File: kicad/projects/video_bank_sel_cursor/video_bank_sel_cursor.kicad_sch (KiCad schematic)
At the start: 44 parts, among them J1 peripheral_addr_bus_connector, J2 peripheral_aux_connector, J3 peripheral_membank_connector, J4 Conn_01x16_Socket, J5 Conn_01x16_Socket, J6 video_aux, J7 Conn_01x16_Socket, J8 Conn_01x06_Socket, U1 74HC245, U10 74HC10, U11 74HC377, U12 74HC377, U14 74HC245, U15 74HC245, U2 74HC245, U3 74HC245, U4 74HC245, U5 74HC245, U6 74HC245, U7 74HC245, U8 74HC245, U9 74HC10

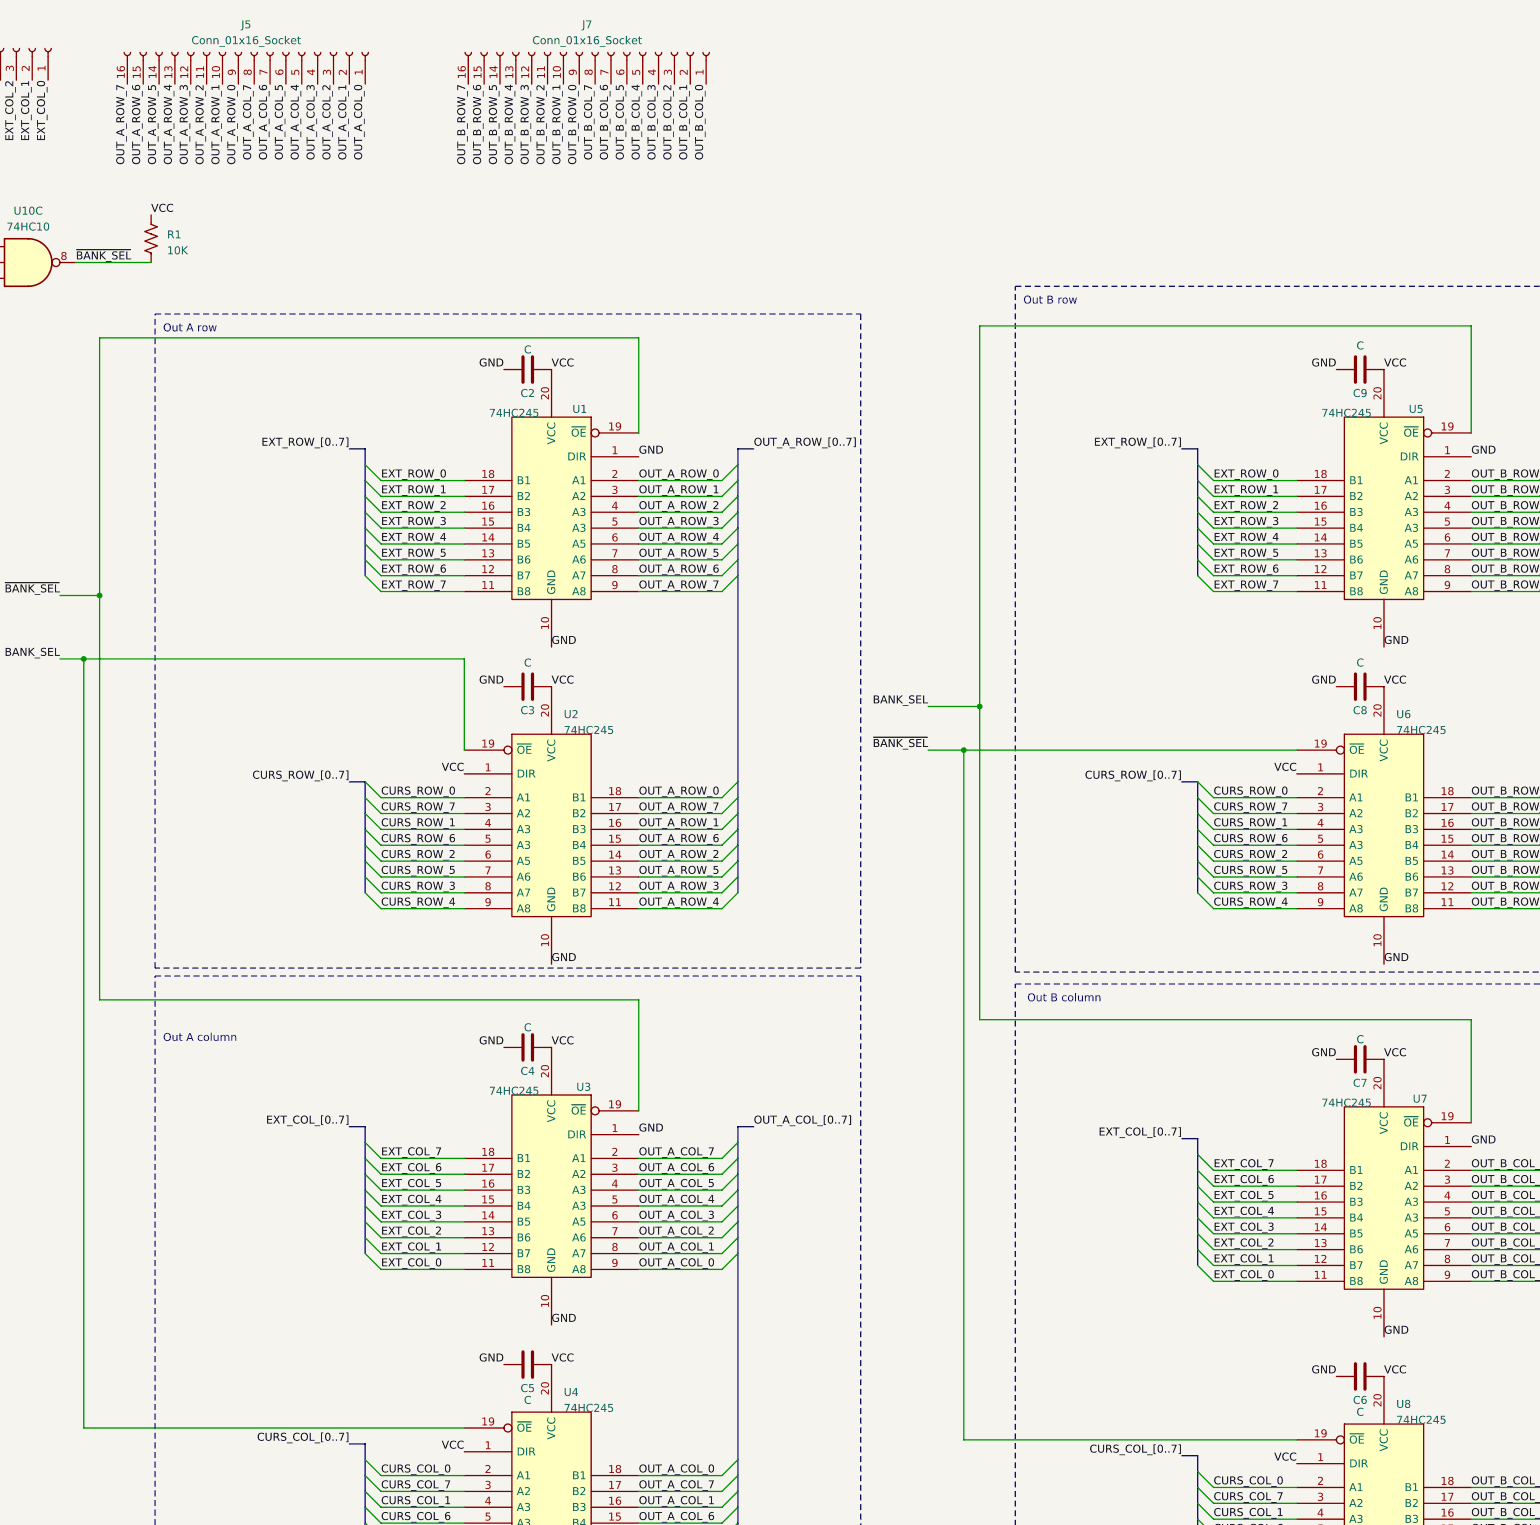
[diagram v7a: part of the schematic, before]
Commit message: Switched A and B outputs on bank sel. Bit of work on logic and PCB for output. Clarified bank sel 0 and 1 and banks A and B in docs.
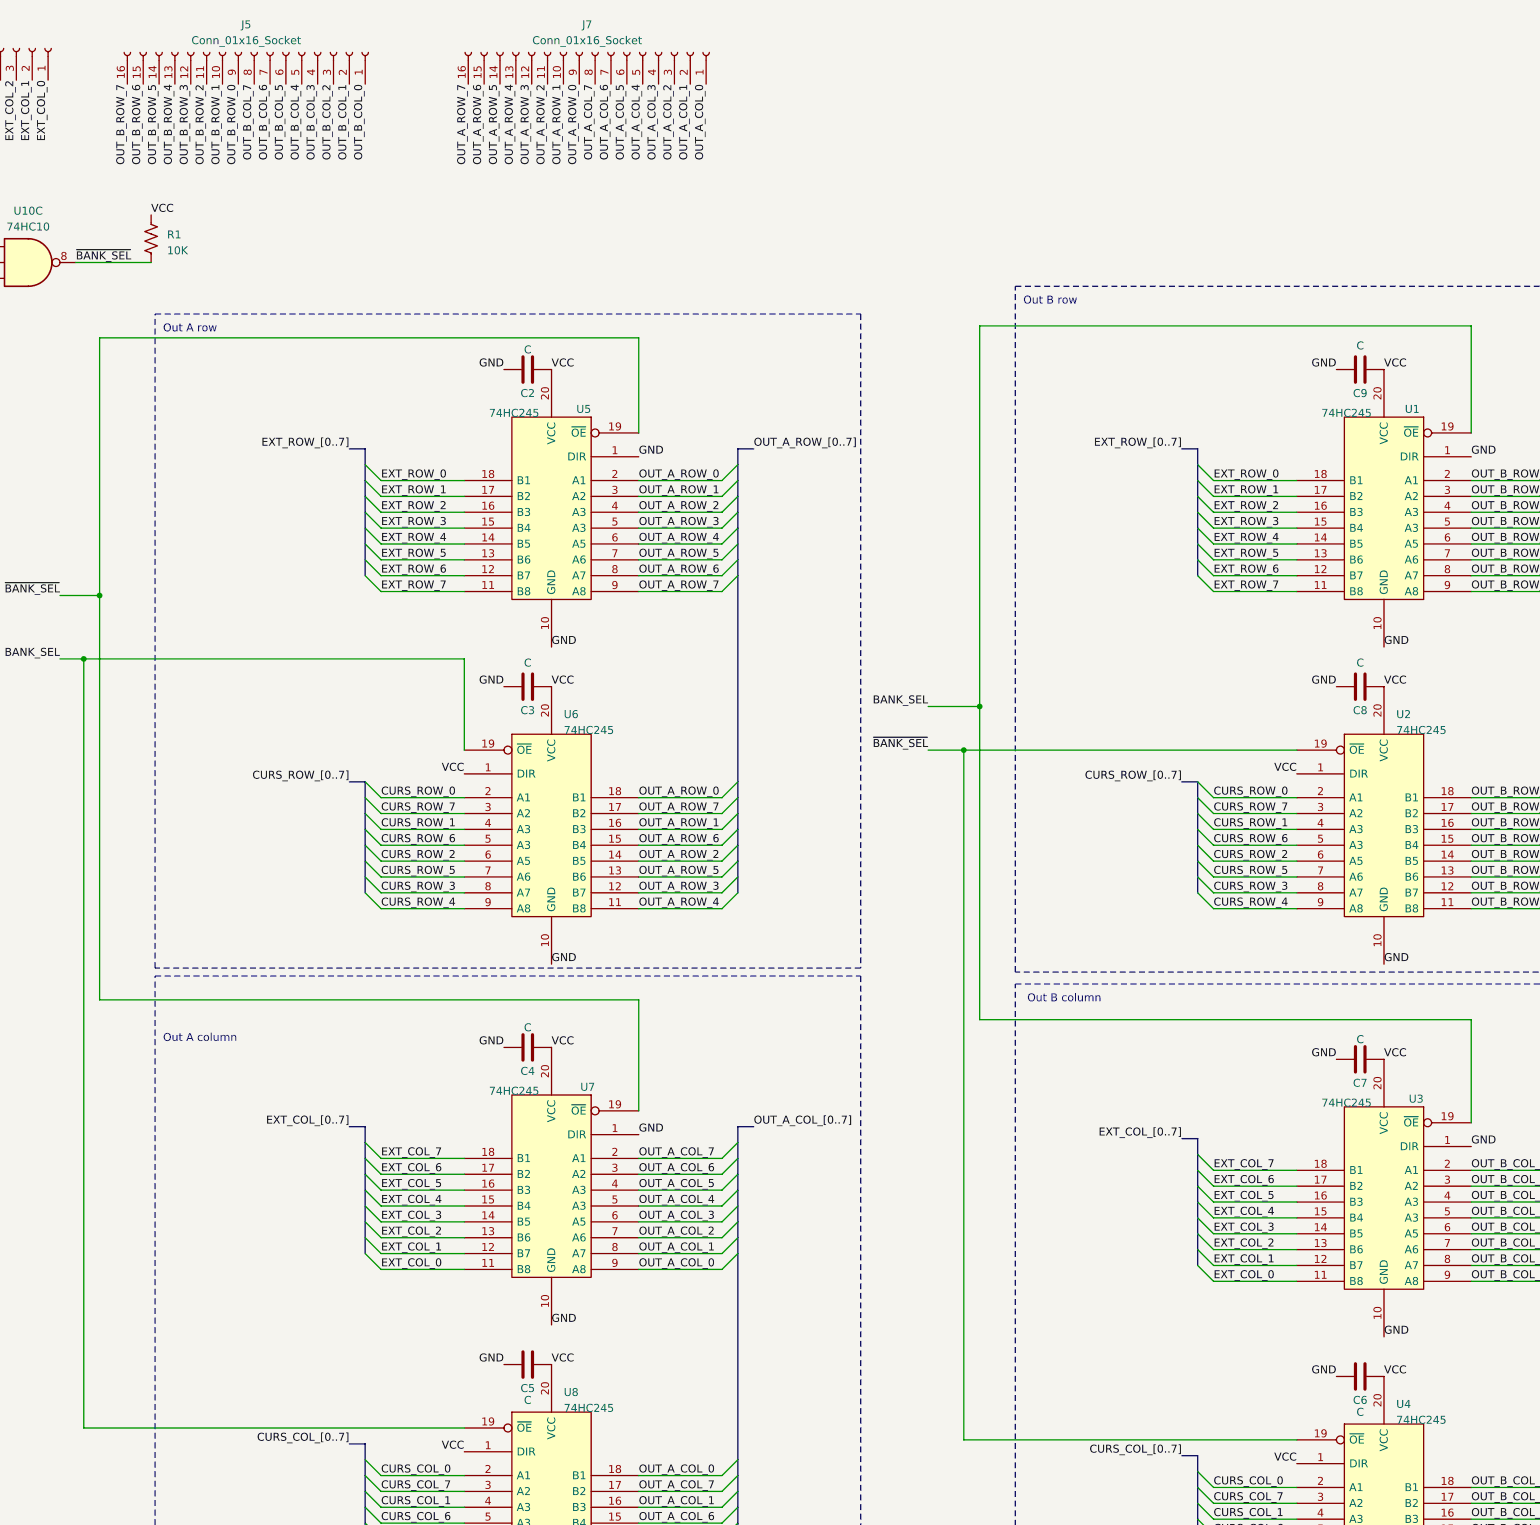
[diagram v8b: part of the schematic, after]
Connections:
- net BANK_SEL: now also U1.19 (~{OE}), U3.19 (~{OE}), U6.19 (~{OE}), U8.19 (~{OE}); no longer U2.19 (~{OE}), U4.19 (~{OE}), U5.19 (~{OE}), U7.19 (~{OE})
- net OUT_A_COL_0: now also J7.1 (Pin_1), U7.9 (A8), U8.18 (B1); no longer J5.1 (Pin_1), U3.9 (A8), U4.18 (B1)
- net OUT_A_COL_1: now also J7.2 (Pin_2), U7.8 (A7), U8.16 (B3); no longer J5.2 (Pin_2), U3.8 (A7), U4.16 (B3)
- net OUT_A_COL_2: now also J7.3 (Pin_3), U7.7 (A6), U8.14 (B5); no longer J5.3 (Pin_3), U3.7 (A6), U4.14 (B5)
- net OUT_A_COL_3: now also J7.4 (Pin_4), U7.6 (A5), U8.12 (B7); no longer J5.4 (Pin_4), U3.6 (A5), U4.12 (B7)
- net OUT_A_COL_4: now also J7.5 (Pin_5), U7.5 (A3), U8.11 (B8); no longer J5.5 (Pin_5), U3.5 (A3), U4.11 (B8)
- net OUT_A_COL_5: now also J7.6 (Pin_6), U7.4 (A3), U8.13 (B6); no longer J5.6 (Pin_6), U3.4 (A3), U4.13 (B6)
- net OUT_A_COL_6: now also J7.7 (Pin_7), U7.3 (A2), U8.15 (B4); no longer J5.7 (Pin_7), U3.3 (A2), U4.15 (B4)
- net OUT_A_COL_7: now also J7.8 (Pin_8), U7.2 (A1), U8.17 (B2); no longer J5.8 (Pin_8), U3.2 (A1), U4.17 (B2)
- net OUT_A_ROW_0: now also J7.9 (Pin_9), U5.2 (A1), U6.18 (B1); no longer J5.9 (Pin_9), U1.2 (A1), U2.18 (B1)
- net OUT_A_ROW_1: now also J7.10 (Pin_10), U5.3 (A2), U6.16 (B3); no longer J5.10 (Pin_10), U1.3 (A2), U2.16 (B3)
- net OUT_A_ROW_2: now also J7.11 (Pin_11), U5.4 (A3), U6.14 (B5); no longer J5.11 (Pin_11), U1.4 (A3), U2.14 (B5)
- net OUT_A_ROW_3: now also J7.12 (Pin_12), U5.5 (A3), U6.12 (B7); no longer J5.12 (Pin_12), U1.5 (A3), U2.12 (B7)
- net OUT_A_ROW_4: now also J7.13 (Pin_13), U5.6 (A5), U6.11 (B8); no longer J5.13 (Pin_13), U1.6 (A5), U2.11 (B8)
- net OUT_A_ROW_5: now also J7.14 (Pin_14), U5.7 (A6), U6.13 (B6); no longer J5.14 (Pin_14), U1.7 (A6), U2.13 (B6)
- net OUT_A_ROW_6: now also J7.15 (Pin_15), U5.8 (A7), U6.15 (B4); no longer J5.15 (Pin_15), U1.8 (A7), U2.15 (B4)
- net OUT_A_ROW_7: now also J7.16 (Pin_16), U5.9 (A8), U6.17 (B2); no longer J5.16 (Pin_16), U1.9 (A8), U2.17 (B2)
- net OUT_B_COL_0: now also J5.1 (Pin_1), U3.9 (A8), U4.18 (B1); no longer J7.1 (Pin_1), U7.9 (A8), U8.18 (B1)
- net OUT_B_COL_1: now also J5.2 (Pin_2), U3.8 (A7), U4.16 (B3); no longer J7.2 (Pin_2), U7.8 (A7), U8.16 (B3)
- net OUT_B_COL_2: now also J5.3 (Pin_3), U3.7 (A6), U4.14 (B5); no longer J7.3 (Pin_3), U7.7 (A6), U8.14 (B5)
- net OUT_B_COL_3: now also J5.4 (Pin_4), U3.6 (A5), U4.12 (B7); no longer J7.4 (Pin_4), U7.6 (A5), U8.12 (B7)
- net OUT_B_COL_4: now also J5.5 (Pin_5), U3.5 (A3), U4.11 (B8); no longer J7.5 (Pin_5), U7.5 (A3), U8.11 (B8)
- net OUT_B_COL_5: now also J5.6 (Pin_6), U3.4 (A3), U4.13 (B6); no longer J7.6 (Pin_6), U7.4 (A3), U8.13 (B6)
- net OUT_B_COL_6: now also J5.7 (Pin_7), U3.3 (A2), U4.15 (B4); no longer J7.7 (Pin_7), U7.3 (A2), U8.15 (B4)
- net OUT_B_COL_7: now also J5.8 (Pin_8), U3.2 (A1), U4.17 (B2); no longer J7.8 (Pin_8), U7.2 (A1), U8.17 (B2)
- net OUT_B_ROW_0: now also J5.9 (Pin_9), U1.2 (A1), U2.18 (B1); no longer J7.9 (Pin_9), U5.2 (A1), U6.18 (B1)
- net OUT_B_ROW_1: now also J5.10 (Pin_10), U1.3 (A2), U2.16 (B3); no longer J7.10 (Pin_10), U5.3 (A2), U6.16 (B3)
- net OUT_B_ROW_2: now also J5.11 (Pin_11), U1.4 (A3), U2.14 (B5); no longer J7.11 (Pin_11), U5.4 (A3), U6.14 (B5)
- net OUT_B_ROW_3: now also J5.12 (Pin_12), U1.5 (A3), U2.12 (B7); no longer J7.12 (Pin_12), U5.5 (A3), U6.12 (B7)
- net OUT_B_ROW_4: now also J5.13 (Pin_13), U1.6 (A5), U2.11 (B8); no longer J7.13 (Pin_13), U5.6 (A5), U6.11 (B8)
- net OUT_B_ROW_5: now also J5.14 (Pin_14), U1.7 (A6), U2.13 (B6); no longer J7.14 (Pin_14), U5.7 (A6), U6.13 (B6)
- net OUT_B_ROW_6: now also J5.15 (Pin_15), U1.8 (A7), U2.15 (B4); no longer J7.15 (Pin_15), U5.8 (A7), U6.15 (B4)
- net OUT_B_ROW_7: now also J5.16 (Pin_16), U1.9 (A8), U2.17 (B2); no longer J7.16 (Pin_16), U5.9 (A8), U6.17 (B2)
- net ~{BANK_SEL}: now also U2.19 (~{OE}), U4.19 (~{OE}), U5.19 (~{OE}), U7.19 (~{OE}); no longer U1.19 (~{OE}), U3.19 (~{OE}), U6.19 (~{OE}), U8.19 (~{OE})
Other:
- moved on the sheet: U1, U2, U3, U4, U5, U6, U7, U8
